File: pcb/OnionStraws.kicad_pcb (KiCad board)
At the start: 2 copper layers, 100 x 50 mm, 46 parts, among them J1 Conn_01x04, J2 8P8C, Q1 Si2309CDS, Q2 Si2309CDS, U1 74LVC2G07, U2 74LVC2G07_3v3, U3 ESP32, U4 APX803L

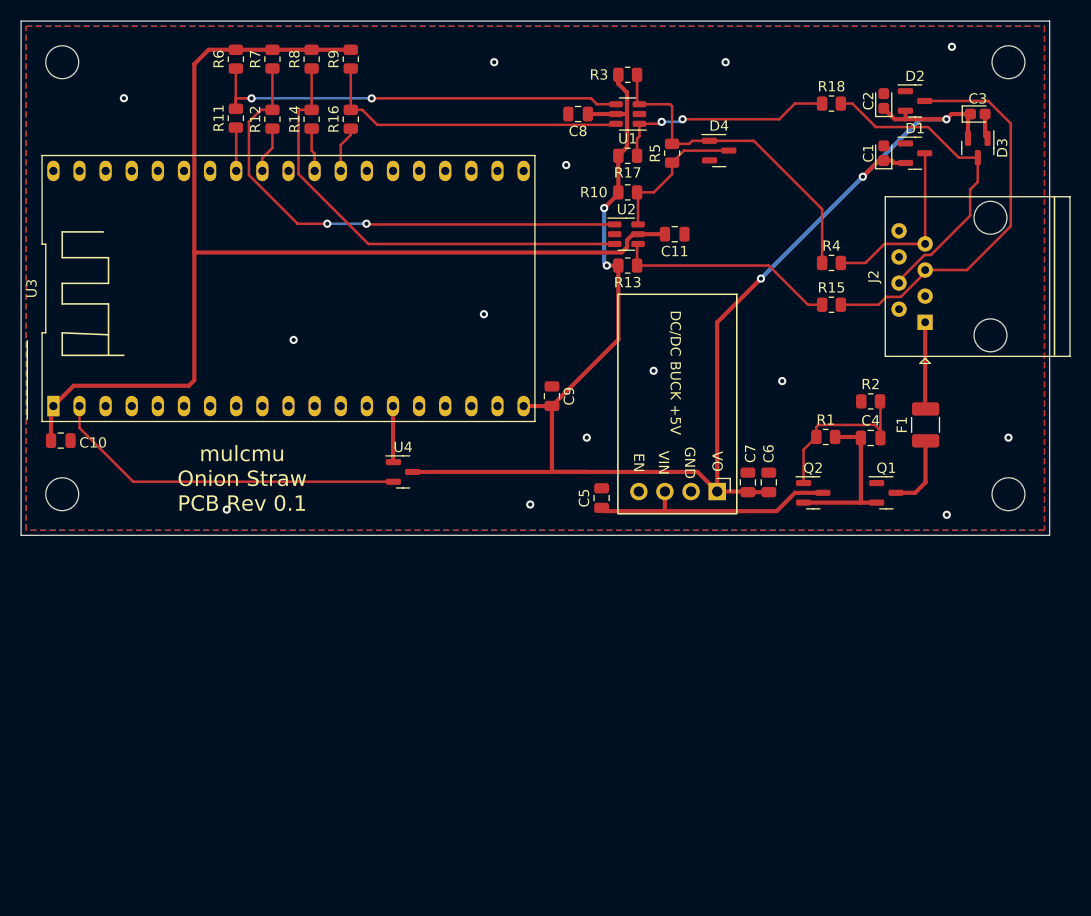
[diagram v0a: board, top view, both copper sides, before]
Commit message: Rev 0.2 PCB
Fix unconnected GND pads
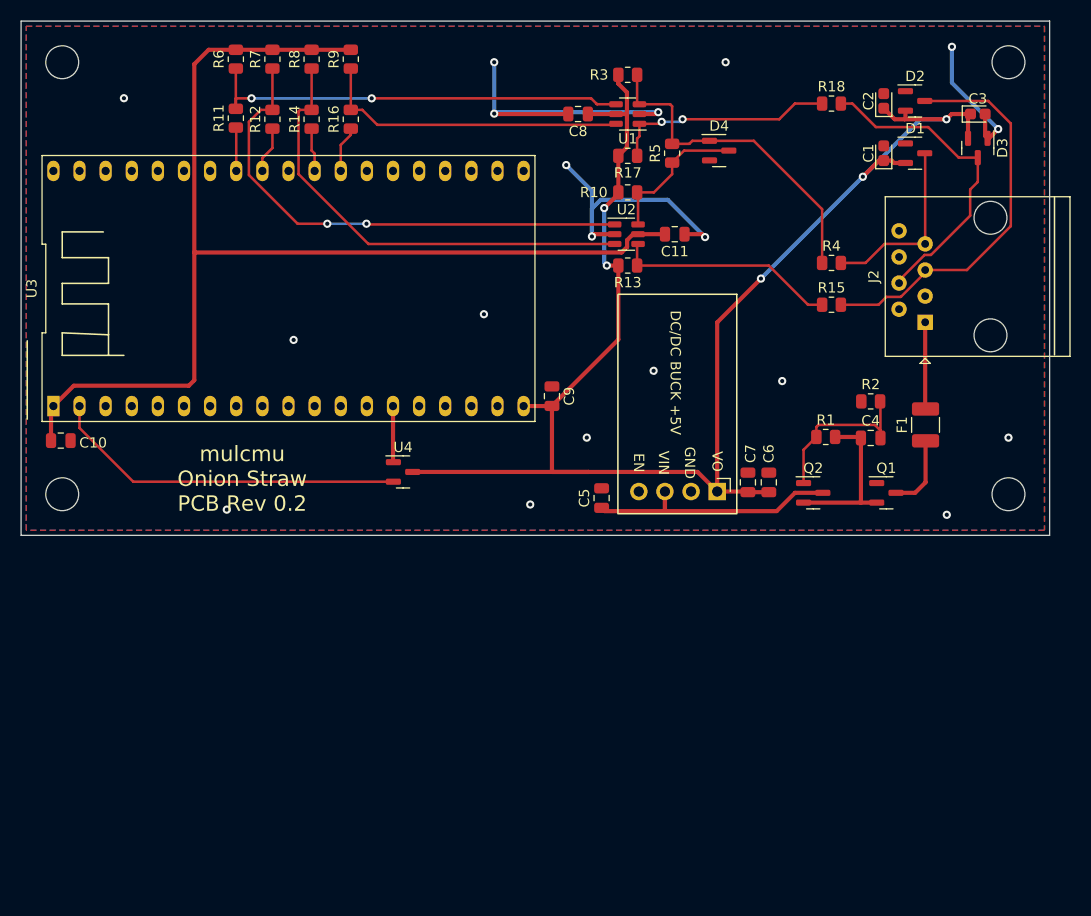
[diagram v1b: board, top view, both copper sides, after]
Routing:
- net GND: track 7.93 -> 77.3 mm, vias 14 -> 19
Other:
- board text added: "mulcmu Onion Straw PCB Rev 0.2"
- board text removed: "mulcmu Onion Straw PCB Rev 0.1"

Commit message: PCB Rev 0.3
Fixed D4 and related pull up resistors.
Added LED and PB
Added 5V zener diode and TVS for input
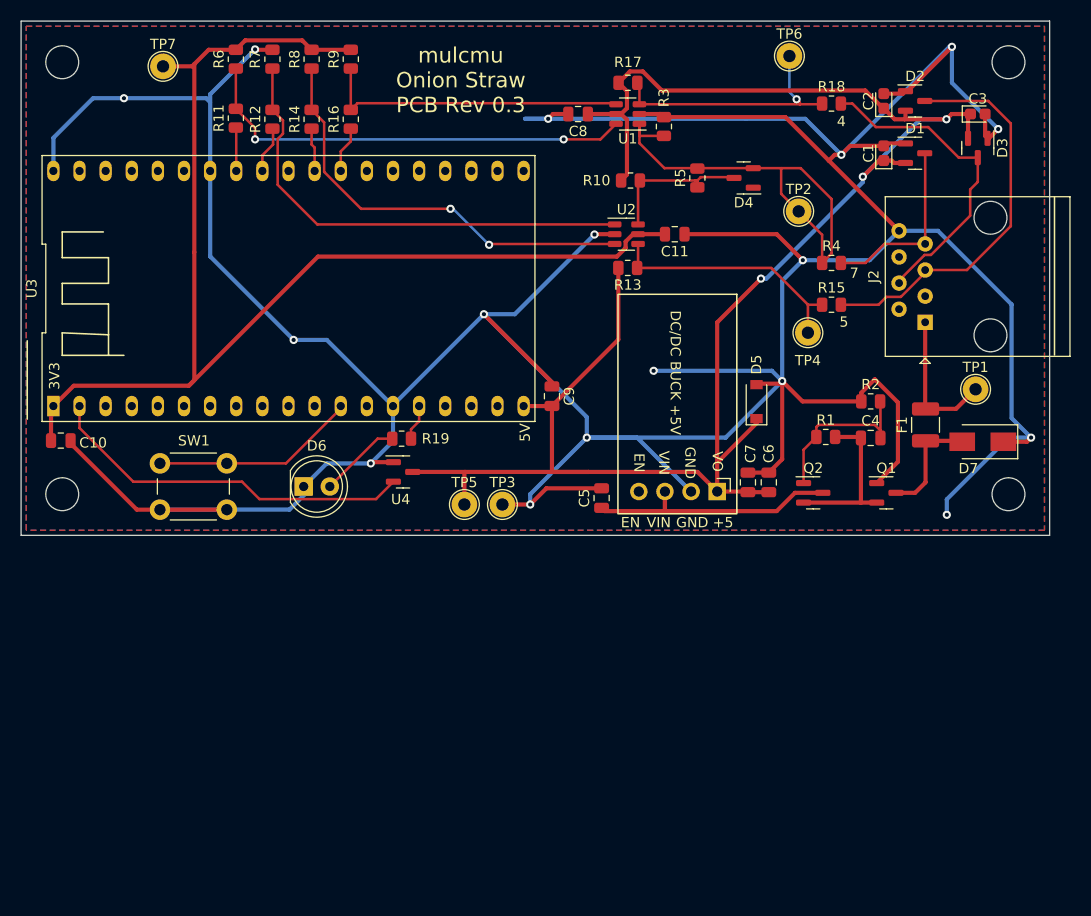
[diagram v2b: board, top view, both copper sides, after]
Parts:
- added D5: 5.2V, Diode_SMD:D_SOD-123, F.Cu at (106.5, 62.0)
- added D6: LED, LED_THT:LED_D5.0mm, F.Cu at (62.5, 70.2)
- added D7: D_TVS, Diode_SMD:D_SMA, F.Cu at (128.5, 65.9)
- added R19: 220, Resistor_SMD:R_0805_2012Metric, F.Cu at (72.0, 65.6)
- added SW1: SW_Push, Button_Switch_THT:SW_PUSH_6mm_H13mm, F.Cu at (55.0, 72.5)
- added TP1: TestPoint, TestPoint:TestPoint_THTPad_D2.5mm_Drill1.2mm, F.Cu at (127.8, 60.8)
- added TP2: TestPoint, TestPoint:TestPoint_THTPad_D2.5mm_Drill1.2mm, F.Cu at (110.6, 43.5)
- added TP3: TestPoint, TestPoint:TestPoint_THTPad_D2.5mm_Drill1.2mm, F.Cu at (81.8, 72.0)
- added TP4: TestPoint, TestPoint:TestPoint_THTPad_D2.5mm_Drill1.2mm, F.Cu at (111.5, 55.3)
- added TP5: TestPoint, TestPoint:TestPoint_THTPad_D2.5mm_Drill1.2mm, F.Cu at (78.1, 72.0)
- added TP6: TestPoint, TestPoint:TestPoint_THTPad_D2.5mm_Drill1.2mm, F.Cu at (109.7, 28.4)
- added TP7: TestPoint, TestPoint:TestPoint_THTPad_D2.5mm_Drill1.2mm, F.Cu at (48.8, 29.4)
- C1, C2, C3: value 0.1u -> 100n
- C5: value 100u -> 10u
- R17, R3: value 250k -> 270k
- moved R17 7.10 mm to (94.0, 31.0)
- moved R3 6.13 mm to (97.5, 35.2), turned to 90 degrees
- moved D4 3.57 mm to (105.2, 40.2), turned to 180 degrees
- moved R5 3.43 mm to (100.8, 40.2)
- moved R10 1.19 mm to (94.2, 40.5)
- moved R13 0.23 mm to (94.0, 49.0)
- turned R7 to -90 degrees
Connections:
- D4 pad 1: Net-(D4-Pad1) -> unconnected-(D4-Pad1)
- D4 pad 2: unconnected-(D4-Pad2) -> Net-(D4-Pad2)
- R3 pad 1: Net-(D4-Pad1) -> Net-(D4-Pad2)
- R3 pad 2: +5V -> GND
- R4 pad 1: Net-(D4-Pad1) -> Net-(D4-Pad2)
- R5 pad 2: Net-(D4-Pad1) -> Net-(D4-Pad2)
- R7 pad 1: Net-(R12-Pad2) -> GND
- R7 pad 2: +3V3 -> Net-(R12-Pad2)
- U1 pad 1: Net-(R17-Pad1) -> Net-(D4-Pad2)
- U1 pad 3: Net-(D4-Pad1) -> Net-(R17-Pad1)
- U1 pad 4: Net-(R11-Pad2) -> Net-(R16-Pad2)
- U1 pad 6: Net-(R16-Pad2) -> Net-(R11-Pad2)
- U3 pad 12: unconnected-(U3-Pad12) -> Net-(SW1-Pad2)
- U3 pad 15: unconnected-(U3-Pad15) -> Net-(R19-Pad2)
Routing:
- net GND: track 77.3 -> 464.9 mm, vias 19 -> 17
- net Net-(D4-Pad2): track 0.00 -> 43.8 mm
- net Net-(D4-Pad1): track 32.6 -> 0.00 mm
- net +5V: track 153.6 -> 179.2 mm, vias 5 -> 3
- net Net-(SW1-Pad2): track 0.00 -> 20.0 mm
- net +3V3: track 111.6 -> 121.4 mm
- net Net-(D6-Pad2): track 0.00 -> 8.00 mm
- net VDC: track 8.44 -> 14.1 mm
- net /p1: track 7.33 -> 10.9 mm
- net Net-(R19-Pad2): track 0.00 -> 3.50 mm
- net Net-(R17-Pad1): track 21.8 -> 25.1 mm, vias 2 -> 1
- net Net-(R14-Pad2): track 45.0 -> 41.8 mm, vias 0 -> 2
- net Net-(R12-Pad2): track 49.5 -> 46.3 mm, vias 2 -> 0
- net Net-(R13-Pad1): track 21.7 -> 24.6 mm
- net Net-(U3-Pad2): track 34.8 -> 36.2 mm
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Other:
- board text added: "+5"
- board text added: "3V3"
- board text added: "4"
- board text added: "5"
- board text added: "5V"
- board text added: "7"
- board text added: "EN"
- board text added: "GND"
- board text added: "VIN"
- board text added: "mulcmu Onion Straw PCB Rev 0.3"
- board text removed: "mulcmu Onion Straw PCB Rev 0.2"

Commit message: PCB Rev 1.0
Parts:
- added R77: 270k, Resistor_SMD:R_0805_2012Metric, F.Cu at (102.4, 33.9)
- added R88: 10K, Resistor_SMD:R_0805_2012Metric, F.Cu at (62.5, 28.8)
- added R99: 10K, Resistor_SMD:R_0805_2012Metric, F.Cu at (73.5, 28.7)
- moved R16 4.06 mm to (71.1, 34.5)
- moved R9 4.06 mm to (71.1, 28.7)
- moved R14 4.06 mm to (67.3, 34.5)
- moved R8 4.06 mm to (67.3, 28.7)
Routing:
- net GND: track 464.9 -> 481.7 mm, vias 17 -> 18
- net Net-(R14-Pad2): track 41.8 -> 48.6 mm
- net Net-(R16-Pad1): track 4.52 -> 8.66 mm
- net +3V3: track 121.4 -> 125.4 mm
- net Net-(R16-Pad2): track 30.1 -> 27.2 mm
- net Net-(R14-Pad1): track 4.24 -> 6.51 mm
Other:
- board text added: "mulcmu Onion Straw PCB Rev 1.0"
- board text removed: "mulcmu Onion Straw PCB Rev 0.3"

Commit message: v2 beta
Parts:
- removed H3, H4: MountingHole, MountingHole:MountingHole_3.2mm_M3_DIN965
- removed R77: 270k, Resistor_SMD:R_0805_2012Metric
- removed R88, R99: 10K, Resistor_SMD:R_0805_2012Metric
- removed TP3, TP7: TestPoint, TestPoint:TestPoint_THTPad_D2.5mm_Drill1.2mm
- added C12: 100n, Capacitor_SMD:C_0805_2012Metric, F.Cu at (81.5, 106.0)
- added C13: 10u, Capacitor_SMD:C_0805_2012Metric, F.Cu at (80.5, 103.0)
- added C14: 100n, Capacitor_SMD:C_0805_2012Metric, F.Cu at (76.5, 103.0)
- added D8: 5.2V, Diode_SMD:D_SOD-523, F.Cu at (82.8, 109.0)
- added D9: BAV99, Package_TO_SOT_SMD:SOT-23, F.Cu at (96.3, 85.9)
- added F2: Polyfuse, Fuse:Fuse_1812_4532Metric, F.Cu at (121.0, 106.5)
- added INPUT POWER: TestPoint, TestPoint:TestPoint_Pad_D2.0mm, B.Cu at (109.5, 104.6)
- added J3: TC2030, Connector:Tag-Connect_TC2030-IDC-NL_2x03_P1.27mm_Vertical, B.Cu at (50.7, 107.4)
- added JP1: FirstBuild, Jumper:SolderJumper-3_P1.3mm_Bridged12_RoundedPad1.0x1.5mm_NumberLabels, B.Cu at (59.5, 103.8)
- added Power Pin: AltPwr, Jumper:SolderJumper-3_P1.3mm_Bridged12_RoundedPad1.0x1.5mm_NumberLabels, B.Cu at (115.5, 106.5)
- added R20: 10K, Resistor_SMD:R_0805_2012Metric, F.Cu at (81.3, 95.1)
- added R21: 220k, Resistor_SMD:R_0805_2012Metric, F.Cu at (90.7, 92.3)
- added R22: 4K7, Resistor_SMD:R_0805_2012Metric, F.Cu at (99.0, 82.8)
- added R23: 1K, Resistor_SMD:R_0805_2012Metric, F.Cu at (103.6, 82.8)
- added R24: 1K, Resistor_SMD:R_0805_2012Metric, F.Cu at (103.6, 85.8)
- added R25: 1K, Resistor_SMD:R_0805_2012Metric, F.Cu at (103.6, 89.8)
- added SW2: SW_Push, Button_Switch_SMD:SW_Push_1P1T_XKB_TS-1187A, F.Cu at (67.0, 104.5)
- added U5: 74LVC2G07_3v3, Package_TO_SOT_SMD:SOT-23-6, F.Cu at (76.9, 90.5)
- added U6: AP2205-3.3, Package_TO_SOT_SMD:SOT-89-3, F.Cu at (76.5, 107.0)
- C1, C3: footprint Capacitor_Tantalum_SMD:CP_EIA-1608-10_AVX-L -> Capacitor_SMD:C_0805_2012Metric
- C10, C5, C6: value 10u -> 100n
- C11, C9: value 100n -> 10u
- C2: value 100n -> 1u; footprint Capacitor_Tantalum_SMD:CP_EIA-1608-10_AVX-L -> Capacitor_SMD:C_0805_2012Metric
- C4, C7: value 1u -> 100n
- C8: value 100n -> 1u
- D4: value BAV99 -> GRN; footprint Package_TO_SOT_SMD:SOT-23 -> LED_SMD:LED_0805_2012Metric
- D5: value 5.2V -> RED; footprint Diode_SMD:D_SOD-123 -> LED_SMD:LED_0805_2012Metric
- D6: value LED -> YLW; footprint LED_THT:LED_D5.0mm -> LED_SMD:LED_0805_2012Metric
- F1: footprint Resistor_SMD:R_1210_3225Metric_Pad1.30x2.65mm_HandSolder -> Fuse:Fuse_1812_4532Metric
- J1: value Conn_01x04 -> 8P8C; footprint Connector_PinHeader_2.54mm:PinHeader_1x04_P2.54mm_Horizontal -> Connector_RJ:RJ45_Amphenol_54602-x08_Horizontal
- J2: value 8P8C -> 1x6; footprint Connector_RJ:RJ45_Amphenol_54602-x08_Horizontal -> Connector_PinHeader_2.54mm:PinHeader_1x06_P2.54mm_Vertical; moved to B.Cu
- R1: value DNP -> 10K
- R10, R13: value 10K -> 1K
- R14, R15, R16: value 1K -> 10K
- R17, R3: value 270k -> 10K
- R18: value 1K -> 220k
- R19: value 220 -> 10K
- R2: value 1M -> 10K
- R4: value 1K -> 220
- R5: value 4K7 -> 10K
- R6, R7: value 10K -> 220
- R8: value 10K -> DNP; moved to B.Cu
- R9: value 10K -> 1M
- SW1: footprint Button_Switch_THT:SW_PUSH_6mm_H13mm -> Button_Switch_SMD:SW_Push_1P1T_XKB_TS-1187A
- TP1, TP2, TP4, TP5, TP6: footprint TestPoint:TestPoint_THTPad_D2.5mm_Drill1.2mm -> TestPoint:TestPoint_Pad_D2.0mm; moved to B.Cu
- U1: value 74LVC2G07 -> APX803L20-29SA-7; footprint Package_TO_SOT_SMD:SOT-23-6 -> Package_TO_SOT_SMD:SOT-23
- U2: value 74LVC2G07_3v3 -> ESP32-C3-WROOM-02; footprint Package_TO_SOT_SMD:SOT-23-6 -> RF_Module:ESP32-C3-WROOM-02
- U3: value ESP32 -> L7805; footprint Library:DIP-38_900_ELL -> Package_TO_SOT_SMD:TO-263-2
- U4: value APX803L -> 74LVC2G07; footprint Package_TO_SOT_SMD:SOT-23 -> Package_TO_SOT_SMD:SOT-23-6
- moved C2 104.0 mm to (44.9, 105.8), turned to 0 degrees
- moved R8 90.0 mm to (109.4, 108.2), turned to 0 degrees
- moved U1 85.1 mm to (50.6, 107.3), turned to 90 degrees
- moved C4 84.3 mm to (45.0, 108.2), turned to 180 degrees
- moved R3 81.7 mm to (59.0, 107.3), turned to -90 degrees
- moved R9 81.6 mm to (107.9, 101.5), turned to 180 degrees
- moved J2 78.5 mm to (58.0, 98.5)
- moved R4 77.2 mm to (44.6, 82.7), turned to 90 degrees
- moved R2 76.0 mm to (56.6, 107.3), turned to 90 degrees
- moved C8 74.1 mm to (105.0, 106.5), turned to 90 degrees
- moved H1 70.9 mm to (65.0, 95.0)
- moved H2 68.8 mm to (103.5, 95.0)
- moved R5 68.7 mm to (46.8, 82.7)
- moved D4 66.8 mm to (53.7, 82.7), turned to 90 degrees
- moved U2 66.1 mm to (49.7, 94.9), turned to 90 degrees
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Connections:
- C10 pad 1: +3V3 -> GND
- C10 pad 2: GND -> /p3
- C11 pad 1: GND -> +5V
- C11 pad 2: +3V3 -> GND
- C2 pad 1: +5V -> +3V3
- C4 pad 1: /p2 -> GND
- C4 pad 2: Net-(C4-Pad2) -> +3V3
- C5 pad 1: /p3 -> +5V
- C6 pad 1: +5V -> GND
- C6 pad 2: GND -> +3V3
- C8 pad 1: +5V -> /p2
- C8 pad 2: GND -> Net-(Q2-G)
- C9 pad 1: GND -> /p3
- C9 pad 2: +5V -> GND
- D4 pad 1: unconnected-(D4-Pad1) -> GND
- D4 pad 2: Net-(D4-Pad2) -> Net-(D4-A)
- D5 pad 1: +5V -> /DBG_LED
- D5 pad 2: GND -> Net-(D5-A)
- D6 pad 2: Net-(D6-Pad2) -> Net-(D6-A)
- F1 pad 1: /p1 -> /ALT_PWR
- F1 pad 2: VDC -> Net-(JP2-B)
- J1 pad 1: +5V -> VDC
- J1 pad 2: GND -> unconnected-(J1-Pad2)
- J1 pad 3: /p3 -> /ALT_PWR
- J1 pad 4: unconnected-(J1-Pad4) -> GEA_FullTx
- J2 pad 1: VDC -> +3V3
- J2 pad 2: unconnected-(J2-Pad2) -> GND
- J2 pad 3: unconnected-(J2-Pad3) -> /BOOT
- J2 pad 4: GEA_FullTx -> GEA3_TX
- J2 pad 5: GEA_FullRx -> GEA3_RX
- J2 pad 6: unconnected-(J2-Pad6) -> /EN
- Q2 pad 1: Net-(C4-Pad2) -> Net-(Q2-G)
- R1 pad 1: Net-(C4-Pad2) -> /BOOT_SEL
- R1 pad 2: /p2 -> +3V3
- R10 pad 1: Net-(D4-Pad3) -> GEA2_RX
- R10 pad 2: +5V -> Net-(R10-Pad2)
- R11 pad 1: Net-(R11-Pad1) -> GEA2_TX
- R12 pad 1: Net-(R12-Pad1) -> GEA3_RX
- R13 pad 1: Net-(R13-Pad1) -> GEA3_TX
- R13 pad 2: +5V -> Net-(R13-Pad2)
- R14 pad 1: Net-(R14-Pad1) -> Net-(R10-Pad2)
- R14 pad 2: Net-(R14-Pad2) -> +3V3
- R15 pad 1: Net-(R13-Pad1) -> GND
- R15 pad 2: GEA_FullRx -> Net-(R11-Pad2)
- R16 pad 1: Net-(R16-Pad1) -> Net-(R12-Pad2)
- R16 pad 2: Net-(R16-Pad2) -> +3V3
- R17 pad 1: Net-(R17-Pad1) -> Net-(R13-Pad2)
- R17 pad 2: +5V -> +3V3
- R18 pad 1: Net-(R17-Pad1) -> Net-(D9-A)
- R18 pad 2: GEA_FullTx -> GND
- R19 pad 1: Net-(D6-Pad2) -> Net-(D9-K-Pad3)
- R19 pad 2: Net-(R19-Pad2) -> +5V
- R2 pad 1: GND -> +3V3
- R2 pad 2: Net-(C4-Pad2) -> /BOOT
- R3 pad 1: Net-(D4-Pad2) -> /EN
- R3 pad 2: GND -> +3V3
- R4 pad 1: Net-(D4-Pad2) -> Net-(D5-A)
- R4 pad 2: GEA_HalfDplx -> +3V3
- R5 pad 1: Net-(D4-Pad3) -> /DBG_LED
- R5 pad 2: Net-(D4-Pad2) -> +3V3
- R6 pad 1: Net-(R11-Pad2) -> /LED2
- R6 pad 2: +3V3 -> Net-(D4-A)
- R7 pad 1: GND -> Net-(D6-A)
- R7 pad 2: Net-(R12-Pad2) -> /LED1
- R8 pad 1: Net-(R14-Pad2) -> Net-(Q2-G)
- R8 pad 2: +3V3 -> /p2
- R9 pad 1: Net-(R16-Pad2) -> GND
- R9 pad 2: +3V3 -> Net-(Q2-G)
- SW1 pad 1: GND -> /BOOT_SEL
- SW1 pad 2: Net-(SW1-Pad2) -> GND
- TP1 pad 1: VDC -> +5V
- TP2 pad 1: Net-(D4-Pad2) -> +3V3
- TP4 pad 1: Net-(R13-Pad1) -> Net-(D9-A)
- TP5 pad 1: +5V -> Net-(R20-Pad1)
- TP6 pad 1: Net-(R17-Pad1) -> Net-(R21-Pad1)
- U1 pad 1: Net-(D4-Pad2) -> GND
- U1 pad 2: GND -> /EN
- U1 pad 3: Net-(R17-Pad1) -> +3V3
- U2 pad 1: Net-(R12-Pad2) -> +3V3
- U2 pad 2: GND -> /EN
- U2 pad 3: Net-(R14-Pad2) -> /LED1
- U2 pad 4: Net-(R13-Pad1) -> Net-(JP1-A)
- U2 pad 5: +3V3 -> unconnected-(U2-IO6-Pad5)
- U2 pad 6: Net-(D4-Pad3) -> unconnected-(U2-IO7-Pad6)
- U3 pad 1: +3V3 -> /p3
- U3 pad 2: Net-(U3-Pad2) -> GND
- U3 pad 3: unconnected-(U3-Pad3) -> +5V
- U4 pad 1: GND -> Net-(D9-A)
- U4 pad 2: Net-(U3-Pad2) -> GND
- U4 pad 3: +5V -> Net-(R21-Pad1)
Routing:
- net GND: track 481.7 -> 358.9 mm, vias 18 -> 34
- net +3V3: track 125.4 -> 196.2 mm, vias 0 -> 6
- net GEA3_RX: track 0.00 -> 61.0 mm, vias 0 -> 1
- net GEA3_TX: track 0.00 -> 54.9 mm
- net +5V: track 179.2 -> 126.3 mm, vias 3 -> 6
- net /BOOT_SEL: track 0.00 -> 51.3 mm, vias 0 -> 2
- net Net-(R14-Pad2): track 48.6 -> 0.00 mm, vias 2 -> 0
- net Net-(D4-Pad2): track 43.8 -> 0.00 mm
- net /BOOT: track 0.00 -> 38.4 mm, vias 0 -> 2
- net Net-(R12-Pad2): track 46.3 -> 8.35 mm
- net Net-(R20-Pad1): track 0.00 -> 37.0 mm, vias 0 -> 3
- net Net-(U3-Pad2): track 36.2 -> 0.00 mm
- net Net-(R21-Pad1): track 0.00 -> 33.6 mm, vias 0 -> 3
- net Net-(R11-Pad2): track 43.4 -> 10.4 mm, vias 2 -> 0
- net /EN: track 0.00 -> 31.9 mm, vias 0 -> 3
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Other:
- board size 100 x 50 mm -> 88.6 x 30 mm
- board text added: "3v3 GND BOOT EN RX TX"
- board text added: "5V 3v3 Half (7) Full RX (5) Full TX (4)"
- board text added: "DIY Wi-fi adapter for GEA2 and GEA3 Connect to appliance at your own risk!"
- board text added: "EN RX TX BOOT GND 3v3"
- board text added: "mulcmu Onion Straws Revision 2.0"
- board text removed: "+5"
- board text removed: "3V3"
- board text removed: "4"
- board text removed: "5"
- board text removed: "5V"
- board text removed: "7"
- board text removed: "EN"
- board text removed: "GND"
- board text removed: "VIN"
- board text removed: "mulcmu Onion Straw PCB Rev 1.0"

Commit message: pcb 2.1 mods
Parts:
- added TP7: TestPoint, TestPoint:TestPoint_Pad_D2.0mm, B.Cu at (117.6, 83.8)
- D8: footprint Diode_SMD:D_SOD-523 -> Diode_SMD:D_SOD-123
- JP2: renamed from Power Pin
- TP3: renamed from INPUT POWER
- moved C9 0.30 mm to (84.0, 102.2)
- moved C11 0.25 mm to (84.0, 105.8)
- moved C12 0.25 mm to (81.5, 105.8)
- moved D8 0.20 mm to (82.8, 108.8)
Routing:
- net GND: track 358.9 -> 357.3 mm
- net +5V: track 126.3 -> 125.3 mm
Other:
- board text added: "5V 3v3 Half (7) Full RX (5) Full TX (4) GND"
- board text added: "mulcmu Onion Straws Revision 2.1"
- board text removed: "5V 3v3 Half (7) Full RX (5) Full TX (4)"
- board text removed: "mulcmu Onion Straws Revision 2.0"
